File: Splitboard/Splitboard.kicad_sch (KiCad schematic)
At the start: 0 parts

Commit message: Schema changes
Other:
- note added: "Splitboard ECE 477 Group 4 Final Project"
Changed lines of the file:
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@@
     (stroke (width 0) (type default) (color 0 0 0 0))
+  )
+  (text "Splitboard\nECE 477 Group 4 Final Project" (at 93.218 118.11 0)
+    (effects (font (size 4 4)) (justify left bottom))
   )
   (sheet (at 59.69 27.686) (size 22.098 51.562) (fields_autoplaced)

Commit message: Added Joe's suggestions & notes to schematic & pcb
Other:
- sheet Side A ports: added none; removed VDD
- sheet Side B ports: added VBUS; removed VDD
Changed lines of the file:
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@@
       (effects (font (size 1.27 1.27)) (justify right))
     )
-    (pin "VDD" output (at 81.788 29.972 0)
+    (pin "VBUS" output (at 81.788 29.972 0)
       (effects (font (size 1.27 1.27)) (justify right))
     )
@@
       (effects (font (size 1.27 1.27)) (justify left))
     )
-    (pin "VDD" input (at 116.078 29.972 180)
+    (pin "VBUS" input (at 116.078 29.972 180)
       (effects (font (size 1.27 1.27)) (justify left))
     )
@@
       (reference "#PWR03") (unit 1) (value "+3.3V") (footprint "")
     )
-    (path "/5672c33b-f17a-4447-b73b-6e8ae8b6c0d5/437506f4-9c95-4981-b82e-2fe5deb41c0d"
-      (reference "#PWR04") (unit 1) (value "+3.3V") (footprint "")
-    )
     (path "/5672c33b-f17a-4447-b73b-6e8ae8b6c0d5/661a6976-5c5b-4e1c-82b9-30cd8398a1f3"
       (reference "#PWR05") (unit 1) (value "+3.3V") (footprint "")
@@
       (reference "#PWR015") (unit 1) (value "GND") (footprint "")
     )
-    (path "/5672c33b-f17a-4447-b73b-6e8ae8b6c0d5/4f7a1831-db97-48ac-9791-9eb545408ff2"
-      (reference "#PWR016") (unit 1) (value "GND") (footprint "")
-    )
     (path "/5672c33b-f17a-4447-b73b-6e8ae8b6c0d5/1fc4cf08-e09c-4ca8-8cc5-235537f87343"
       (reference "#PWR017") (unit 1) (value "GND") (footprint "")
@@
       (reference "#PWR019") (unit 1) (value "GND") (footprint "")
     )
-    (path "/5672c33b-f17a-4447-b73b-6e8ae8b6c0d5/0cc4e007-7b6a-47e3-b5eb-dfb650832116"
-      (reference "#PWR020") (unit 1) (value "+3.3V") (footprint "")
-    )
     (path "/5672c33b-f17a-4447-b73b-6e8ae8b6c0d5/7429d2c3-c87d-4560-9b14-127cee99a4bb"
       (reference "#PWR021") (unit 1) (value "GND") (footprint "")
@@
       (reference "#PWR038") (unit 1) (value "GND") (footprint "")
     )
+    (path "/5672c33b-f17a-4447-b73b-6e8ae8b6c0d5/15241e33-bf3e-46c6-a4e6-a0f1a9ce345a"
+      (reference "#PWR?") (unit 1) (value "+3.3V") (footprint "")
+    )
+    (path "/5672c33b-f17a-4447-b73b-6e8ae8b6c0d5/6934f02c-40f5-4e42-aa32-4495ee818187"
+      (reference "#PWR?") (unit 1) (value "VBUS") (footprint "")
+    )
+    (path "/5672c33b-f17a-4447-b73b-6e8ae8b6c0d5/716b6344-e87e-4cc0-bb9c-d256e3ae75e0"
+      (reference "#PWR?") (unit 1) (value "VBUS") (footprint "")
+    )
+    (path "/5672c33b-f17a-4447-b73b-6e8ae8b6c0d5/d059d8e6-9636-4ae0-bc55-09555a84561c"
+      (reference "#PWR?") (unit 1) (value "VBUS") (footprint "")
+    )
+    (path "/5672c33b-f17a-4447-b73b-6e8ae8b6c0d5/dabcd109-c5eb-42ff-a8b7-32851b7ff3b3"
+      (reference "#PWR?") (unit 1) (value "GND") (footprint "")
+    )
+    (path "/5672c33b-f17a-4447-b73b-6e8ae8b6c0d5/e1fe3c09-6a3e-48b0-966a-c183a01ea1e6"
+      (reference "#PWR?") (unit 1) (value "+3.3V") (footprint "")
+    )
     (path "/5672c33b-f17a-4447-b73b-6e8ae8b6c0d5/2c1d7c25-4e6a-4efd-91be-81a9a2df6c69"
       (reference "C1") (unit 1) (value "0.1uF") (footprint "Resistor_SMD:R_0805_2012Metric")
@@
     )
     (path "/5672c33b-f17a-4447-b73b-6e8ae8b6c0d5/8b3f13d3-5769-43a6-8723-b39c4885138a"
-      (reference "C4") (unit 1) (value ".01uF") (footprint "")
+      (reference "C4") (unit 1) (value ".01uF") (footprint "Capacitor_SMD:C_0805_2012Metric")
     )
     (path "/5672c33b-f17a-4447-b73b-6e8ae8b6c0d5/8482c7d2-bb36-4693-84c5-adb75f8e7249"
-      (reference "C5") (unit 1) (value ".01uF") (footprint "")
+      (reference "C5") (unit 1) (value ".01uF") (footprint "Capacitor_SMD:C_0805_2012Metric")
     )
     (path "/5672c33b-f17a-4447-b73b-6e8ae8b6c0d5/680154ad-bbec-4819-b490-9d44ecd5b996"
-      (reference "C6") (unit 1) (value "100nF") (footprint "")
+      (reference "C6") (unit 1) (value "100nF") (footprint "Capacitor_SMD:C_0805_2012Metric")
     )
     (path "/5672c33b-f17a-4447-b73b-6e8ae8b6c0d5/533a9219-f139-4bce-b92a-cbdd4473f037"
-      (reference "C7") (unit 1) (value "100nF") (footprint "")
+      (reference "C7") (unit 1) (value "100nF") (footprint "Capacitor_SMD:C_0805_2012Metric")
     )
     (path "/5672c33b-f17a-4447-b73b-6e8ae8b6c0d5/01b76f08-df10-4e95-98ff-10c59aee281a"
-      (reference "C8") (unit 1) (value "100nF") (footprint "")
+      (reference "C8") (unit 1) (value "100nF") (footprint "Capacitor_SMD:C_0805_2012Metric")
     )
     (path "/5672c33b-f17a-4447-b73b-6e8ae8b6c0d5/0104be38-10d9-4672-a37c-77d94d69245f"
-      (reference "C9") (unit 1) (value "100nF") (footprint "")
+      (reference "C9") (unit 1) (value "100nF") (footprint "Capacitor_SMD:C_0805_2012Metric")
     )
     (path "/5672c33b-f17a-4447-b73b-6e8ae8b6c0d5/b72f6f2d-a41e-4ce1-8a52-c9e27715a261"
-      (reference "C10") (unit 1) (value "100nF") (footprint "")
+      (reference "C10") (unit 1) (value "100nF") (footprint "Capacitor_SMD:C_0805_2012Metric")
     )
     (path "/5672c33b-f17a-4447-b73b-6e8ae8b6c0d5/17797f54-04fa-4bd8-bf08-71fa074eae68"
-      (reference "C11") (unit 1) (value "100nF") (footprint "")
+      (reference "C11") (unit 1) (value "100nF") (footprint "Capacitor_SMD:C_0805_2012Metric")
     )
     (path "/5672c33b-f17a-4447-b73b-6e8ae8b6c0d5/74da3fcb-e63e-4acf-8bf1-3b70ad0e87ee"
-      (reference "C12") (unit 1) (value "100nF") (footprint "")
+      (reference "C12") (unit 1) (value "100nF") (footprint "Capacitor_SMD:C_0805_2012Metric")
     )
     (path "/5672c33b-f17a-4447-b73b-6e8ae8b6c0d5/6b91b9c0-bb4a-4759-a58a-fafb330d1e0b"
-      (reference "C13") (unit 1) (value "100nF") (footprint "")
+      (reference "C13") (unit 1) (value "100nF") (footprint "Capacitor_SMD:C_0805_2012Metric")
     )
     (path "/5672c33b-f17a-4447-b73b-6e8ae8b6c0d5/c22b9fe4-903e-495c-af95-5dea675520c0"
-      (reference "C14") (unit 1) (value "100nF") (footprint "")
+      (reference "C14") (unit 1) (value "100nF") (footprint "Capacitor_SMD:C_0805_2012Metric")
     )
     (path "/5672c33b-f17a-4447-b73b-6e8ae8b6c0d5/5038ed56-89df-42ff-8620-f14bd4ac1988"
-      (reference "C15") (unit 1) (value "100nF") (footprint "")
+      (reference "C15") (unit 1) (value "100nF") (footprint "Capacitor_SMD:C_0805_2012Metric")
     )
     (path "/5672c33b-f17a-4447-b73b-6e8ae8b6c0d5/765ad625-20e1-4aee-a90a-15d6258bb705"
-      (reference "C16") (unit 1) (value "100nF") (footprint "")
+      (reference "C16") (unit 1) (value "100nF") (footprint "Capacitor_SMD:C_0805_2012Metric")
     )
     (path "/5672c33b-f17a-4447-b73b-6e8ae8b6c0d5/8e3167f0-2f3e-45df-9e04-363549564985"
-      (reference "C17") (unit 1) (value "100nF") (footprint "")
+      (reference "C17") (unit 1) (value "100nF") (footprint "Capacitor_SMD:C_0805_2012Metric")
     )
     (path "/eeedf4ca-d3f7-4489-9e0f-4992ff8d20a1/a7a8845b-0858-41e0-bd13-0430d1b47242"
@@
       (reference "J2") (unit 1) (value "USB_C_Receptacle") (footprint "USB_C_Receptacle_GCT_USB4085")
     )
-    (path "/5672c33b-f17a-4447-b73b-6e8ae8b6c0d5/14643cae-960b-4755-a78a-ecaa7af727b3"
-      (reference "J3") (unit 1) (value "Conn_01x07") (footprint "")
-    )
     (path "/eeedf4ca-d3f7-4489-9e0f-4992ff8d20a1/0b866b2c-59e5-47ab-93d6-af71aa803eac"
       (reference "J4") (unit 1) (value "USB_C_Receptacle") (footprint "USB_C_Receptacle_GCT_USB4085")
     )
+    (path "/5672c33b-f17a-4447-b73b-6e8ae8b6c0d5/8d0eaf72-d08b-4900-9512-9e74bf89528d"
+      (reference "J?") (unit 1) (value "Conn_01x06") (footprint "Connector_PinHeader_2.54mm:PinHeader_1x06_P2.54mm_Horizontal")
+    )
     (path "/5672c33b-f17a-4447-b73b-6e8ae8b6c0d5/00000000-0000-0000-0000-00006051f173"
       (reference "K1") (unit 1) (value "KEYSW") (footprint "6:SW_Hotswap_Kailh_MX_plated")
@@
     )
     (path "/5672c33b-f17a-4447-b73b-6e8ae8b6c0d5/7c9d0033-f8ee-4736-8b27-ff494c147ae8"
-      (reference "R3") (unit 1) (value "10k") (footprint "")
+      (reference "R3") (unit 1) (value "10k") (footprint "Resistor_SMD:R_0805_2012Metric")
     )
     (path "/5672c33b-f17a-4447-b73b-6e8ae8b6c0d5/ab55aa3a-1da8-404f-9ff9-9394650882d8"
-      (reference "R4") (unit 1) (value "10k") (footprint "")
+      (reference "R4") (unit 1) (value "10k") (footprint "Resistor_SMD:R_0805_2012Metric")
     )
     (path "/5672c33b-f17a-4447-b73b-6e8ae8b6c0d5/8c8833da-2f8f-43d3-9cc0-03b058b2e413"
-      (reference "R5") (unit 1) (value "10k") (footprint "")
+      (reference "R5") (unit 1) (value "10k") (footprint "Resistor_SMD:R_0805_2012Metric")
     )
     (path "/5672c33b-f17a-4447-b73b-6e8ae8b6c0d5/9140fac7-c5b1-4a6d-90ee-87584346a4f9"
-      (reference "R6") (unit 1) (value "10k") (footprint "")
+      (reference "R6") (unit 1) (value "10k") (footprint "Resistor_SMD:R_0805_2012Metric")
     )
     (path "/eeedf4ca-d3f7-4489-9e0f-4992ff8d20a1/d2a3d573-3fdc-446c-83c0-323323c0f869"
@@
       (reference "R12") (unit 1) (value "10k") (footprint "")
     )
+    (path "/5672c33b-f17a-4447-b73b-6e8ae8b6c0d5/82eb7027-3b9f-407e-842f-1eb2adf56e01"
+      (reference "R?") (unit 1) (value "10K") (footprint "")
+    )
     (path "/5672c33b-f17a-4447-b73b-6e8ae8b6c0d5/38fe4bc3-8fec-480e-9eda-33bcbef5df4c"
       (reference "SW1") (unit 1) (value "RotaryEncoder") (footprint "Rotary_Encoder:RotaryEncoder_Alps_EC12E_Vertical_H20mm")
     )
     (path "/5672c33b-f17a-4447-b73b-6e8ae8b6c0d5/aae1d1b8-ecea-4dc3-9e3b-62424a309ff4"
-      (reference "SW2") (unit 1) (value "SW_Push") (footprint "")
+      (reference "SW2") (unit 1) (value "SW_Push") (footprint "Button_Switch_THT:SW_PUSH_6mm")
     )
     (path "/eeedf4ca-d3f7-4489-9e0f-4992ff8d20a1/92527856-d3ca-4bc5-b4fe-d85867977214"

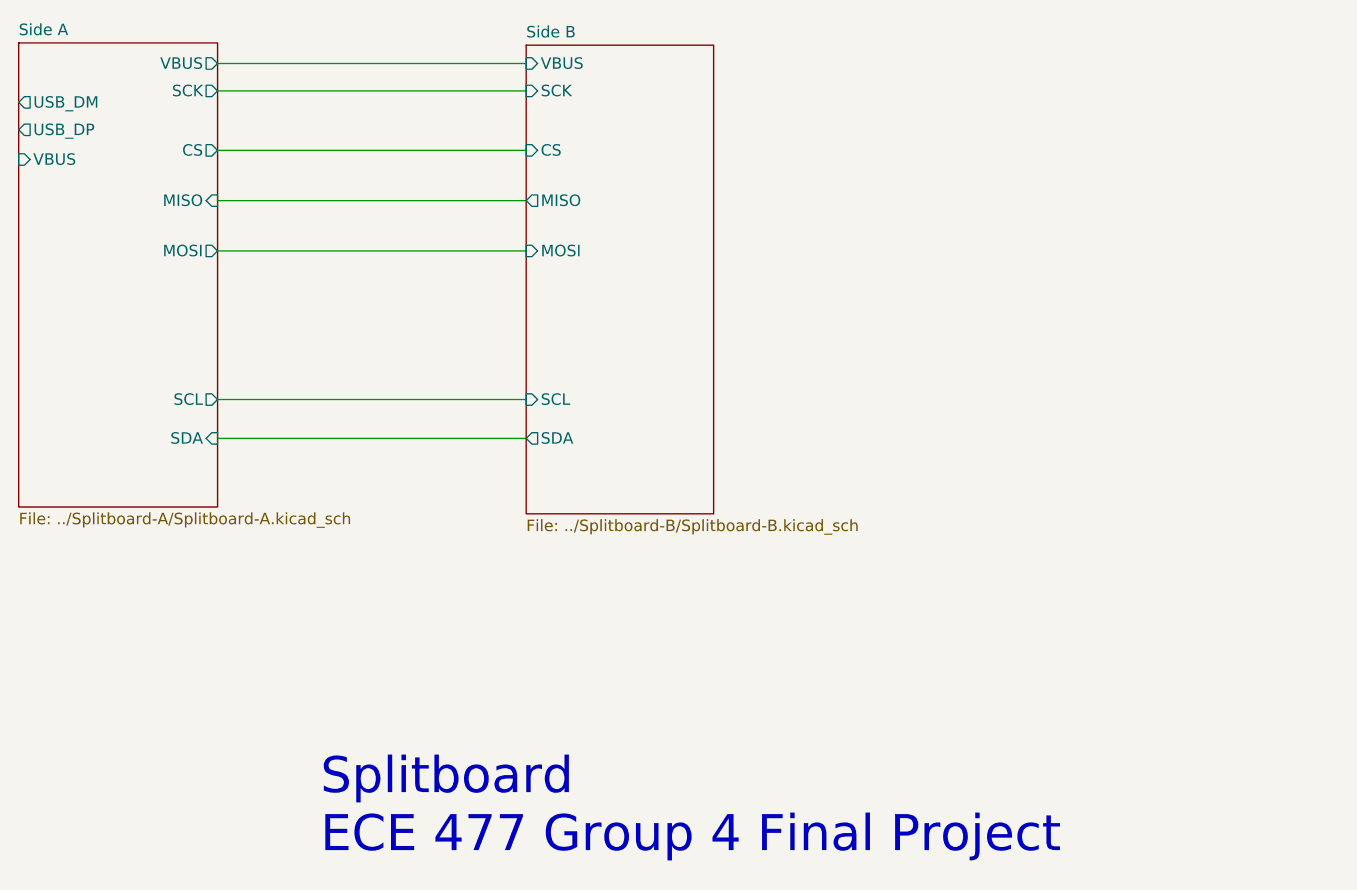
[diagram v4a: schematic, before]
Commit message: updated USB, LCD, ESD, Voltage Reg in schematic
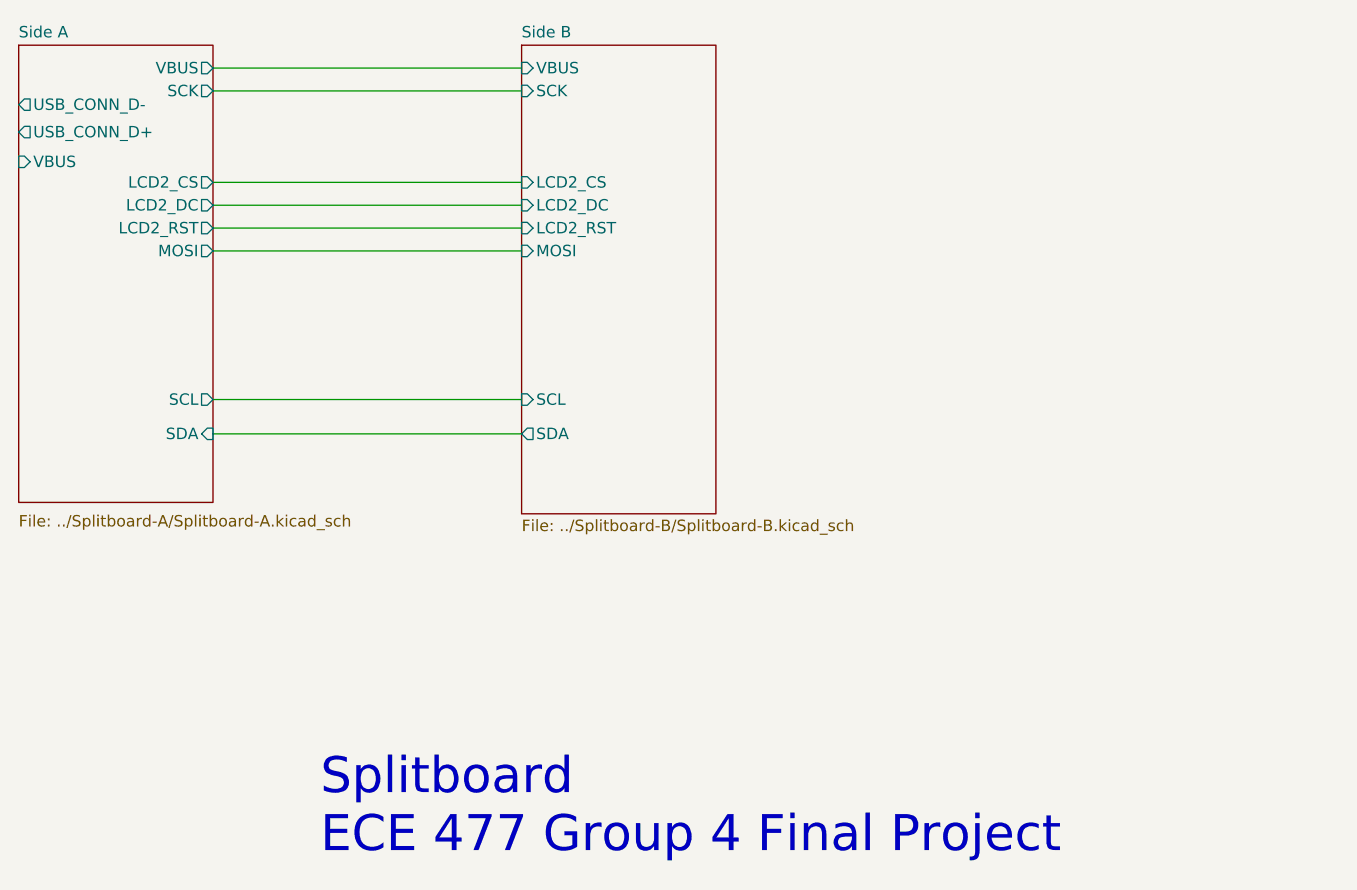
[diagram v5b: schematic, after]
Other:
- sheet Side A ports: added LCD2_CS, LCD2_DC, LCD2_RST, USB_CONN_D+, USB_CONN_D-; removed CS, MISO, USB_DM, USB_DP
- sheet Side B ports: added LCD2_CS, LCD2_DC, LCD2_RST; removed CS, MISO
